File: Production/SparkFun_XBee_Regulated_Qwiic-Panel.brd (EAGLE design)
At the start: 127.8 x 177.8 mm, 870 parts, among them J13 QWIIC_RIGHT_ANGLE, J19 QWIIC_RIGHT_ANGLE, J25 QWIIC_RIGHT_ANGLE, J31 QWIIC_RIGHT_ANGLE, J37 QWIIC_RIGHT_ANGLE, J4 QWIIC_RIGHT_ANGLE, J43 QWIIC_RIGHT_ANGLE, J49 QWIIC_RIGHT_ANGLE, J7 QWIIC_RIGHT_ANGLE, U1 AP63203, U2 AP63203, U3 AP63203, U4 AP63203, U5 AP63203, U6 AP63203, U7 AP63203, U8 AP63203, U9 AP63203

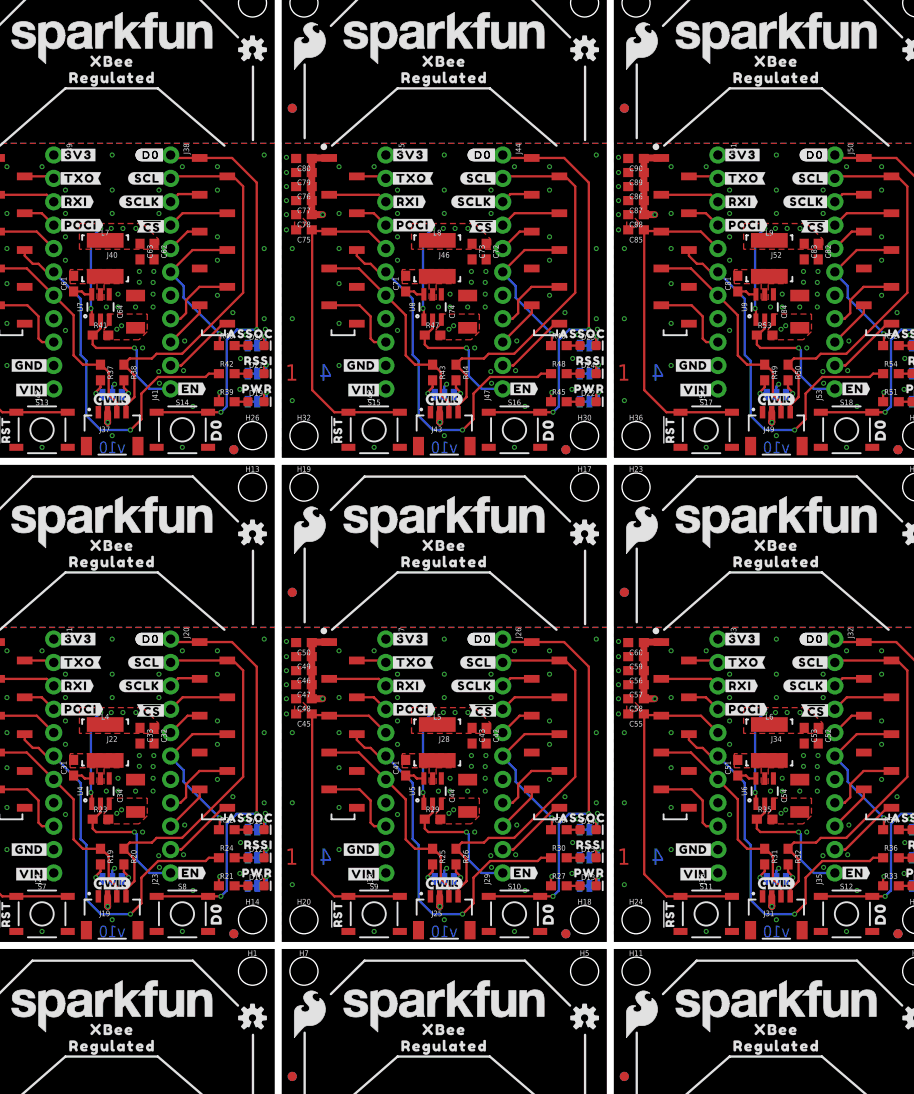
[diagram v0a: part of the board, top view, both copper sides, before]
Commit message: Updates silk on production files
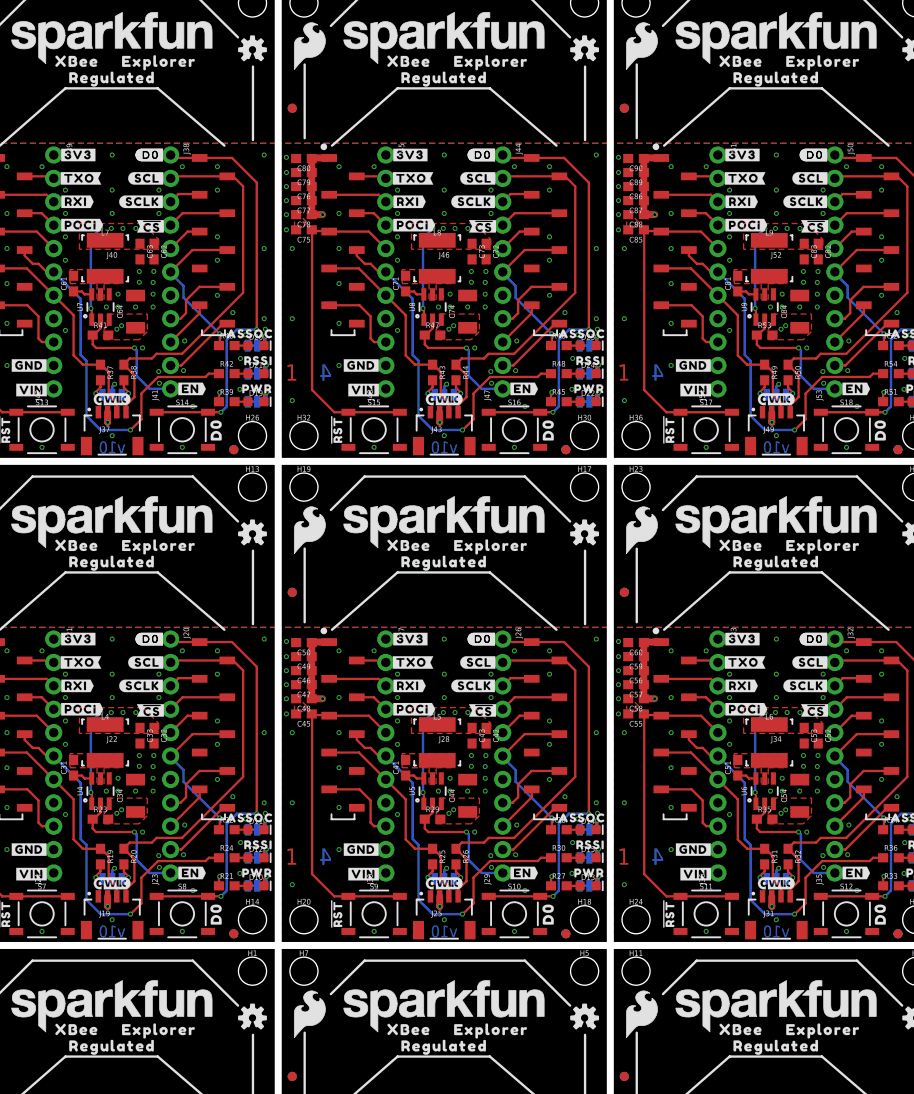
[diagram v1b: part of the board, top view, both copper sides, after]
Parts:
- added U$460: (no value), top:XBEE340
- added U$461: (no value), topmirror:REGULATED1343
- added U$462: (no value), botmirror:#D0#3
- added U$463: (no value), topmirror:#D1#AD1#SCL#8
- added U$464: (no value), topmirror:#RLED#22
- added U$465: (no value), topmirror:#D3#AD3##CS##23
- added U$466: (no value), topmirror:#EN#17
- added U$467, U$468: (no value), topmirror:EXPLORER1344
- U$103, U$260, U$311, U$33: device top:#3V3#1 -> topmirror:EXPLORER1344
- U$104, U$155: device top:#I2C#33 -> topmirror:EXPLORER1344
- U$105: device top:PWR26 -> top:#3V3#1
- U$106: device top:ASSOC27 -> top:#I2C#33
- U$107: device top:#3V3#1 -> top:PWR26
- U$108: device top:#VIN#4 -> top:ASSOC27
- U$109, U$313: device bot:D03 -> top:#3V3#1
- U$110: device top:#RST#30 -> top:#VIN#4
- U$111: device SparkFun-Aesthetics:SFE_LOGO_NAME_.2 -> bot:D03
- U$112: device SparkFun-Aesthetics:SFE_LOGO_FLAME_.2 -> top:#RST#30
- U$113: device top:RSSI31 -> SparkFun-Aesthetics:SFE_LOGO_NAME_.2
- U$114: device topmirror:#D0#AD0#18 -> SparkFun-Aesthetics:SFE_LOGO_FLAME_.2
- U$115: device topmirror:#D2#AD2#19 -> top:RSSI31
- U$116: device topmirror:#D6##RTS##25 -> topmirror:#D0#AD0#18
- U$117: device topmirror:#D5#ASSOC#25 -> topmirror:#D2#AD2#19
- U$118: device topmirror:#D9##SLP##28 -> topmirror:#D6##RTS##25
- U$119: device topmirror:#GND#0 -> topmirror:#D5#ASSOC#25
- U$120: device topmirror:#D8##DTR##27 -> topmirror:#D9##SLP##28
- U$121: device topmirror:#RSSI#D10#17 -> topmirror:#GND#0
- U$122: device topmirror:#SDA#D11#9 -> topmirror:#D8##DTR##27
- U$123: device topmirror:##RST##15 -> topmirror:#RSSI#D10#17
- U$124: device topmirror:#POCI#D12#24 -> topmirror:#SDA#D11#9
- U$125: device topmirror:#RXI#D14#15 -> topmirror:##RST##15
- U$126: device topmirror:#TXO#D13#13 -> topmirror:#POCI#D12#24
- U$127: device topmirror:#ALED#21 -> topmirror:#RXI#D14#15
- U$128: device topmirror:#PLED#20 -> topmirror:#TXO#D13#13
- U$129: device botmirror:#TXO#8 -> topmirror:#ALED#21
- U$130: device botmirror:#RXI#7 -> topmirror:#PLED#20
- U$131: device botmirror:#POCI#32 -> botmirror:#TXO#8
- U$132: device botmirror:##CS##26 -> botmirror:#RXI#7
- U$133: device botmirror:#SCLK#33 -> botmirror:#POCI#32
- U$134: device botmirror:#SCL#9 -> botmirror:##CS##26
- U$135: device botmirror:#D0#3 -> botmirror:#SCLK#33
- U$136: device top:#VIN#4 -> botmirror:#SCL#9
- U$137: device topmirror:#GND#0 -> botmirror:#D0#3
- U$138, U$162: device SparkFun-Aesthetics:SFE_LOGO_NAME_.2 -> top:#VIN#4
- U$139: device topmirror:#EN#17 -> topmirror:#GND#0
- U$140: device topmirror:#NC#1 -> SparkFun-Aesthetics:SFE_LOGO_NAME_.2
- U$141: device botmirror:#NC#3 -> topmirror:#EN#17
- U$142: device top:#D7##CTS##26 -> topmirror:#NC#1
- U$143: device top:#D4#PICO#25 -> botmirror:#NC#3
- U$144, U$352: device topmirror:REGULATED1343 -> top:#D7##CTS##26
- U$145, U$197, U$249: device top:XBEE340 -> top:#D4#PICO#25
- U$146, U$198, U$94: device top:XBEE340 -> topmirror:REGULATED1343
- U$148, U$199: device topmirror:REGULATED1343 -> top:XBEE340
- U$149, U$302: device botmirror:#D0#3 -> topmirror:REGULATED1343
- U$150: device topmirror:#D1#AD1#SCL#8 -> botmirror:#D0#3
- U$151: device topmirror:#RLED#22 -> topmirror:#D1#AD1#SCL#8
- U$152: device topmirror:#D3#AD3##CS##23 -> topmirror:#RLED#22
- U$153: device topmirror:#EN#17 -> topmirror:#D3#AD3##CS##23
- U$154, U$362: device top:#3V3#1 -> topmirror:#EN#17
- U$156, U$207: device top:PWR26 -> topmirror:EXPLORER1344
- U$157: device top:ASSOC27 -> top:#3V3#1
- U$158: device top:#3V3#1 -> top:#I2C#33
- U$159: device top:#VIN#4 -> top:PWR26
- U$160: device bot:D03 -> top:ASSOC27
- U$161, U$365: device top:#RST#30 -> top:#3V3#1
- U$163: device SparkFun-Aesthetics:SFE_LOGO_FLAME_.2 -> bot:D03
- U$164: device top:RSSI31 -> top:#RST#30
- U$165: device topmirror:#D0#AD0#18 -> SparkFun-Aesthetics:SFE_LOGO_NAME_.2
- U$166: device topmirror:#D2#AD2#19 -> SparkFun-Aesthetics:SFE_LOGO_FLAME_.2
- U$167: device topmirror:#D6##RTS##25 -> top:RSSI31
- U$168: device topmirror:#D5#ASSOC#25 -> topmirror:#D0#AD0#18
- U$169: device topmirror:#D9##SLP##28 -> topmirror:#D2#AD2#19
- U$170: device topmirror:#GND#0 -> topmirror:#D6##RTS##25
- U$171: device topmirror:#D8##DTR##27 -> topmirror:#D5#ASSOC#25
- U$172: device topmirror:#RSSI#D10#17 -> topmirror:#D9##SLP##28
- U$173: device topmirror:#SDA#D11#9 -> topmirror:#GND#0
- U$174: device topmirror:##RST##15 -> topmirror:#D8##DTR##27
- U$175: device topmirror:#POCI#D12#24 -> topmirror:#RSSI#D10#17
- U$176: device topmirror:#RXI#D14#15 -> topmirror:#SDA#D11#9
- U$177: device topmirror:#TXO#D13#13 -> topmirror:##RST##15
- U$178: device topmirror:#ALED#21 -> topmirror:#POCI#D12#24
- U$179: device topmirror:#PLED#20 -> topmirror:#RXI#D14#15
- U$180: device botmirror:#TXO#8 -> topmirror:#TXO#D13#13
- U$181: device botmirror:#RXI#7 -> topmirror:#ALED#21
- U$182: device botmirror:#POCI#32 -> topmirror:#PLED#20
- U$183: device botmirror:##CS##26 -> botmirror:#TXO#8
- U$184: device botmirror:#SCLK#33 -> botmirror:#RXI#7
- U$185: device botmirror:#SCL#9 -> botmirror:#POCI#32
- U$186: device botmirror:#D0#3 -> botmirror:##CS##26
- U$187: device top:#VIN#4 -> botmirror:#SCLK#33
- U$188: device topmirror:#GND#0 -> botmirror:#SCL#9
- U$189: device SparkFun-Aesthetics:SFE_LOGO_NAME_.2 -> botmirror:#D0#3
- U$190: device topmirror:#EN#17 -> top:#VIN#4
- U$191: device topmirror:#NC#1 -> topmirror:#GND#0
- U$192: device botmirror:#NC#3 -> SparkFun-Aesthetics:SFE_LOGO_NAME_.2
- U$193: device top:#D7##CTS##26 -> topmirror:#EN#17
- U$194: device top:#D4#PICO#25 -> topmirror:#NC#1
- U$195, U$403: device topmirror:REGULATED1343 -> botmirror:#NC#3
- U$196, U$248, U$300: device top:XBEE340 -> top:#D7##CTS##26
- U$200, U$251: device botmirror:#D0#3 -> top:XBEE340
- U$201, U$354: device topmirror:#D1#AD1#SCL#8 -> topmirror:REGULATED1343
- U$202: device topmirror:#RLED#22 -> botmirror:#D0#3
- U$203: device topmirror:#D3#AD3##CS##23 -> topmirror:#D1#AD1#SCL#8
- U$204: device topmirror:#EN#17 -> topmirror:#RLED#22
- U$205, U$413: device top:#3V3#1 -> topmirror:#D3#AD3##CS##23
- U$206: device top:#I2C#33 -> topmirror:#EN#17
- U$208, U$259: device top:ASSOC27 -> topmirror:EXPLORER1344
- U$210: device top:#VIN#4 -> top:#I2C#33
- U$211: device bot:D03 -> top:PWR26
- U$212: device top:#RST#30 -> top:ASSOC27
- U$213, U$417: device SparkFun-Aesthetics:SFE_LOGO_NAME_.2 -> top:#3V3#1
- U$214: device SparkFun-Aesthetics:SFE_LOGO_FLAME_.2 -> top:#VIN#4
- U$215: device top:RSSI31 -> bot:D03
- U$216: device topmirror:#D0#AD0#18 -> top:#RST#30
- U$217: device topmirror:#D2#AD2#19 -> SparkFun-Aesthetics:SFE_LOGO_NAME_.2
- U$218: device topmirror:#D6##RTS##25 -> SparkFun-Aesthetics:SFE_LOGO_FLAME_.2
- U$219: device topmirror:#D5#ASSOC#25 -> top:RSSI31
- U$220: device topmirror:#D9##SLP##28 -> topmirror:#D0#AD0#18
- U$221: device topmirror:#GND#0 -> topmirror:#D2#AD2#19
- U$222: device topmirror:#D8##DTR##27 -> topmirror:#D6##RTS##25
- U$223: device topmirror:#RSSI#D10#17 -> topmirror:#D5#ASSOC#25
- U$224: device topmirror:#SDA#D11#9 -> topmirror:#D9##SLP##28
- U$225: device topmirror:##RST##15 -> topmirror:#GND#0
- U$226: device topmirror:#POCI#D12#24 -> topmirror:#D8##DTR##27
- U$227: device topmirror:#RXI#D14#15 -> topmirror:#RSSI#D10#17
- U$228: device topmirror:#TXO#D13#13 -> topmirror:#SDA#D11#9
- U$229: device topmirror:#ALED#21 -> topmirror:##RST##15
- U$23: device top:XBEE340 -> topmirror:EXPLORER1344
- U$230: device topmirror:#PLED#20 -> topmirror:#POCI#D12#24
- U$231: device botmirror:#TXO#8 -> topmirror:#RXI#D14#15
- U$232: device botmirror:#RXI#7 -> topmirror:#TXO#D13#13
- U$233: device botmirror:#POCI#32 -> topmirror:#ALED#21
- U$234: device botmirror:##CS##26 -> topmirror:#PLED#20
- U$235: device botmirror:#SCLK#33 -> botmirror:#TXO#8
- U$236: device botmirror:#SCL#9 -> botmirror:#RXI#7
- U$237: device botmirror:#D0#3 -> botmirror:#POCI#32
- U$238: device top:#VIN#4 -> botmirror:##CS##26
- U$239: device topmirror:#GND#0 -> botmirror:#SCLK#33
- U$240: device SparkFun-Aesthetics:SFE_LOGO_NAME_.2 -> botmirror:#SCL#9
- U$241, U$306: device topmirror:#EN#17 -> botmirror:#D0#3
- U$242: device topmirror:#NC#1 -> top:#VIN#4
- U$243: device botmirror:#NC#3 -> topmirror:#GND#0
- U$244: device top:#D7##CTS##26 -> SparkFun-Aesthetics:SFE_LOGO_NAME_.2
- U$245: device top:#D4#PICO#25 -> topmirror:#EN#17
- U$246, U$454: device topmirror:REGULATED1343 -> topmirror:#NC#1
- U$247, U$299, U$351: device top:XBEE340 -> botmirror:#NC#3
- U$252, U$303: device topmirror:#D1#AD1#SCL#8 -> top:XBEE340
- U$253, U$406: device topmirror:#RLED#22 -> topmirror:REGULATED1343
- U$254: device topmirror:#D3#AD3##CS##23 -> botmirror:#D0#3
- U$255: device topmirror:#EN#17 -> topmirror:#D1#AD1#SCL#8
- U$256: device top:#3V3#1 -> topmirror:#RLED#22
- U$257: device top:#I2C#33 -> topmirror:#D3#AD3##CS##23
- U$258: device top:PWR26 -> topmirror:#EN#17
- U$261, U$47: device top:#VIN#4 -> top:#3V3#1
- U$262: device bot:D03 -> top:#I2C#33
- U$263: device top:#RST#30 -> top:PWR26
- U$264: device SparkFun-Aesthetics:SFE_LOGO_NAME_.2 -> top:ASSOC27
- U$265: device SparkFun-Aesthetics:SFE_LOGO_FLAME_.2 -> top:#3V3#1
- U$266: device top:RSSI31 -> top:#VIN#4
- U$267: device topmirror:#D0#AD0#18 -> bot:D03
- U$268: device topmirror:#D2#AD2#19 -> top:#RST#30
- U$269: device topmirror:#D6##RTS##25 -> SparkFun-Aesthetics:SFE_LOGO_NAME_.2
- U$270: device topmirror:#D5#ASSOC#25 -> SparkFun-Aesthetics:SFE_LOGO_FLAME_.2
- U$271: device topmirror:#D9##SLP##28 -> top:RSSI31
- U$272: device topmirror:#GND#0 -> topmirror:#D0#AD0#18
- U$273: device topmirror:#D8##DTR##27 -> topmirror:#D2#AD2#19
- U$274: device topmirror:#RSSI#D10#17 -> topmirror:#D6##RTS##25
- U$275: device topmirror:#SDA#D11#9 -> topmirror:#D5#ASSOC#25
- U$276: device topmirror:##RST##15 -> topmirror:#D9##SLP##28
- U$277: device topmirror:#POCI#D12#24 -> topmirror:#GND#0
- U$278: device topmirror:#RXI#D14#15 -> topmirror:#D8##DTR##27
- U$279: device topmirror:#TXO#D13#13 -> topmirror:#RSSI#D10#17
- U$280: device topmirror:#ALED#21 -> topmirror:#SDA#D11#9
- U$281: device topmirror:#PLED#20 -> topmirror:##RST##15
- U$282: device botmirror:#TXO#8 -> topmirror:#POCI#D12#24
- U$283: device botmirror:#RXI#7 -> topmirror:#RXI#D14#15
- U$284: device botmirror:#POCI#32 -> topmirror:#TXO#D13#13
- U$285: device botmirror:##CS##26 -> topmirror:#ALED#21
- U$286: device botmirror:#SCLK#33 -> topmirror:#PLED#20
- U$287: device botmirror:#SCL#9 -> botmirror:#TXO#8
- U$288: device botmirror:#D0#3 -> botmirror:#RXI#7
- U$289: device top:#VIN#4 -> botmirror:#POCI#32
- U$290: device topmirror:#GND#0 -> botmirror:##CS##26
- U$291: device SparkFun-Aesthetics:SFE_LOGO_NAME_.2 -> botmirror:#SCLK#33
- U$292: device topmirror:#EN#17 -> botmirror:#SCL#9
- U$293: device topmirror:#NC#1 -> botmirror:#D0#3
- U$294: device botmirror:#NC#3 -> top:#VIN#4
- U$295: device top:#D7##CTS##26 -> topmirror:#GND#0
- U$296: device top:#D4#PICO#25 -> SparkFun-Aesthetics:SFE_LOGO_NAME_.2
- U$297: device topmirror:REGULATED1343 -> topmirror:#EN#17
- U$298, U$350, U$402: device top:XBEE340 -> topmirror:#NC#1
- U$301, U$93: device topmirror:REGULATED1343 -> top:#D4#PICO#25
- U$304, U$355: device topmirror:#RLED#22 -> top:XBEE340
- U$305, U$458: device topmirror:#D3#AD3##CS##23 -> topmirror:REGULATED1343
- U$307: device top:#3V3#1 -> topmirror:#D1#AD1#SCL#8
- U$308: device top:#I2C#33 -> topmirror:#RLED#22
- U$309: device top:PWR26 -> topmirror:#D3#AD3##CS##23
- U$310: device top:ASSOC27 -> topmirror:#EN#17
- U$312, U$363: device top:#VIN#4 -> topmirror:EXPLORER1344
- U$314: device top:#RST#30 -> top:#I2C#33
- U$315: device SparkFun-Aesthetics:SFE_LOGO_NAME_.2 -> top:PWR26
- U$316: device SparkFun-Aesthetics:SFE_LOGO_FLAME_.2 -> top:ASSOC27
- U$317: device top:RSSI31 -> top:#3V3#1
- U$318: device topmirror:#D0#AD0#18 -> top:#VIN#4
- U$319: device topmirror:#D2#AD2#19 -> bot:D03
- U$320: device topmirror:#D6##RTS##25 -> top:#RST#30
- U$321: device topmirror:#D5#ASSOC#25 -> SparkFun-Aesthetics:SFE_LOGO_NAME_.2
- U$322: device topmirror:#D9##SLP##28 -> SparkFun-Aesthetics:SFE_LOGO_FLAME_.2
- U$323: device topmirror:#GND#0 -> top:RSSI31
- U$324: device topmirror:#D8##DTR##27 -> topmirror:#D0#AD0#18
- U$325: device topmirror:#RSSI#D10#17 -> topmirror:#D2#AD2#19
- U$326: device topmirror:#SDA#D11#9 -> topmirror:#D6##RTS##25
- U$327: device topmirror:##RST##15 -> topmirror:#D5#ASSOC#25
- U$328: device topmirror:#POCI#D12#24 -> topmirror:#D9##SLP##28
- U$329: device topmirror:#RXI#D14#15 -> topmirror:#GND#0
- U$330: device topmirror:#TXO#D13#13 -> topmirror:#D8##DTR##27
- U$331: device topmirror:#ALED#21 -> topmirror:#RSSI#D10#17
- U$332: device topmirror:#PLED#20 -> topmirror:#SDA#D11#9
- U$333: device botmirror:#TXO#8 -> topmirror:##RST##15
- U$334: device botmirror:#RXI#7 -> topmirror:#POCI#D12#24
- U$335: device botmirror:#POCI#32 -> topmirror:#RXI#D14#15
- U$336: device botmirror:##CS##26 -> topmirror:#TXO#D13#13
- U$337: device botmirror:#SCLK#33 -> topmirror:#ALED#21
- U$338: device botmirror:#SCL#9 -> topmirror:#PLED#20
- U$339: device botmirror:#D0#3 -> botmirror:#TXO#8
- U$340: device top:#VIN#4 -> botmirror:#RXI#7
- U$341: device topmirror:#GND#0 -> botmirror:#POCI#32
- U$342: device SparkFun-Aesthetics:SFE_LOGO_NAME_.2 -> botmirror:##CS##26
- U$343: device topmirror:#EN#17 -> botmirror:#SCLK#33
- U$344: device topmirror:#NC#1 -> botmirror:#SCL#9
- U$345: device botmirror:#NC#3 -> botmirror:#D0#3
- U$346: device top:#D7##CTS##26 -> top:#VIN#4
- U$347: device top:#D4#PICO#25 -> topmirror:#GND#0
- U$348: device topmirror:REGULATED1343 -> SparkFun-Aesthetics:SFE_LOGO_NAME_.2
- U$349, U$401, U$453: device top:XBEE340 -> topmirror:#EN#17
- U$353: device botmirror:#D0#3 -> top:#D4#PICO#25
- U$356, U$407: device topmirror:#D3#AD3##CS##23 -> top:XBEE340
- U$357: device topmirror:#EN#17 -> topmirror:REGULATED1343
- U$358: device top:#3V3#1 -> botmirror:#D0#3
- U$359: device top:#I2C#33 -> topmirror:#D1#AD1#SCL#8
- U$360: device top:PWR26 -> topmirror:#RLED#22
- U$361: device top:ASSOC27 -> topmirror:#D3#AD3##CS##23
- U$364, U$415: device bot:D03 -> topmirror:EXPLORER1344
- U$366: device SparkFun-Aesthetics:SFE_LOGO_NAME_.2 -> top:#I2C#33
- U$367: device SparkFun-Aesthetics:SFE_LOGO_FLAME_.2 -> top:PWR26
- U$368: device top:RSSI31 -> top:ASSOC27
- U$369: device topmirror:#D0#AD0#18 -> top:#3V3#1
- U$37: device top:#I2C#33 -> top:#3V3#1
- U$370: device topmirror:#D2#AD2#19 -> top:#VIN#4
- U$371: device topmirror:#D6##RTS##25 -> bot:D03
- U$372: device topmirror:#D5#ASSOC#25 -> top:#RST#30
- U$373: device topmirror:#D9##SLP##28 -> SparkFun-Aesthetics:SFE_LOGO_NAME_.2
- U$374: device topmirror:#GND#0 -> SparkFun-Aesthetics:SFE_LOGO_FLAME_.2
- U$375: device topmirror:#D8##DTR##27 -> top:RSSI31
- U$376: device topmirror:#RSSI#D10#17 -> topmirror:#D0#AD0#18
- U$377: device topmirror:#SDA#D11#9 -> topmirror:#D2#AD2#19
- U$378: device topmirror:##RST##15 -> topmirror:#D6##RTS##25
- U$379: device topmirror:#POCI#D12#24 -> topmirror:#D5#ASSOC#25
- U$38: device top:PWR26 -> top:#I2C#33
- U$380: device topmirror:#RXI#D14#15 -> topmirror:#D9##SLP##28
- U$381: device topmirror:#TXO#D13#13 -> topmirror:#GND#0
- U$382: device topmirror:#ALED#21 -> topmirror:#D8##DTR##27
- U$383: device topmirror:#PLED#20 -> topmirror:#RSSI#D10#17
- U$384: device botmirror:#TXO#8 -> topmirror:#SDA#D11#9
- U$385: device botmirror:#RXI#7 -> topmirror:##RST##15
- U$386: device botmirror:#POCI#32 -> topmirror:#POCI#D12#24
- U$387: device botmirror:##CS##26 -> topmirror:#RXI#D14#15
- U$388: device botmirror:#SCLK#33 -> topmirror:#TXO#D13#13
- U$389: device botmirror:#SCL#9 -> topmirror:#ALED#21
- U$39: device top:ASSOC27 -> top:PWR26
- U$390: device botmirror:#D0#3 -> topmirror:#PLED#20
- U$391: device top:#VIN#4 -> botmirror:#TXO#8
- U$392: device topmirror:#GND#0 -> botmirror:#RXI#7
- U$393: device SparkFun-Aesthetics:SFE_LOGO_NAME_.2 -> botmirror:#POCI#32
- U$394: device topmirror:#EN#17 -> botmirror:##CS##26
- U$395: device topmirror:#NC#1 -> botmirror:#SCLK#33
- U$396: device botmirror:#NC#3 -> botmirror:#SCL#9
- U$397: device top:#D7##CTS##26 -> botmirror:#D0#3
- U$398: device top:#D4#PICO#25 -> top:#VIN#4
- U$399: device topmirror:REGULATED1343 -> topmirror:#GND#0
- U$400, U$452: device top:XBEE340 -> SparkFun-Aesthetics:SFE_LOGO_NAME_.2
- U$404: device botmirror:#D0#3 -> top:#D7##CTS##26
- U$405: device topmirror:#D1#AD1#SCL#8 -> top:#D4#PICO#25
- U$408, U$459: device topmirror:#EN#17 -> top:XBEE340
- U$409: device top:#3V3#1 -> topmirror:REGULATED1343
- U$41: device top:#3V3#1 -> top:ASSOC27
- U$410: device top:#I2C#33 -> botmirror:#D0#3
- U$411: device top:PWR26 -> topmirror:#D1#AD1#SCL#8
- U$412: device top:ASSOC27 -> topmirror:#RLED#22
- U$414: device top:#VIN#4 -> topmirror:#EN#17
- U$416: device top:#RST#30 -> topmirror:EXPLORER1344
- U$418: device SparkFun-Aesthetics:SFE_LOGO_FLAME_.2 -> top:#I2C#33
- U$419: device top:RSSI31 -> top:PWR26
- U$420: device topmirror:#D0#AD0#18 -> top:ASSOC27
- U$421: device topmirror:#D2#AD2#19 -> top:#3V3#1
- U$422: device topmirror:#D6##RTS##25 -> top:#VIN#4
- U$423: device topmirror:#D5#ASSOC#25 -> bot:D03
- U$424: device topmirror:#D9##SLP##28 -> top:#RST#30
- U$425: device topmirror:#GND#0 -> SparkFun-Aesthetics:SFE_LOGO_NAME_.2
- U$426: device topmirror:#D8##DTR##27 -> SparkFun-Aesthetics:SFE_LOGO_FLAME_.2
- U$427: device topmirror:#RSSI#D10#17 -> top:RSSI31
- U$428: device topmirror:#SDA#D11#9 -> topmirror:#D0#AD0#18
- U$429: device topmirror:##RST##15 -> topmirror:#D2#AD2#19
- U$430: device topmirror:#POCI#D12#24 -> topmirror:#D6##RTS##25
- U$431: device topmirror:#RXI#D14#15 -> topmirror:#D5#ASSOC#25
- U$432: device topmirror:#TXO#D13#13 -> topmirror:#D9##SLP##28
- U$433: device topmirror:#ALED#21 -> topmirror:#GND#0
- U$434: device topmirror:#PLED#20 -> topmirror:#D8##DTR##27
- U$435: device botmirror:#TXO#8 -> topmirror:#RSSI#D10#17
- U$436: device botmirror:#RXI#7 -> topmirror:#SDA#D11#9
- U$437: device botmirror:#POCI#32 -> topmirror:##RST##15
- U$438: device botmirror:##CS##26 -> topmirror:#POCI#D12#24
- U$439: device botmirror:#SCLK#33 -> topmirror:#RXI#D14#15
- U$440: device botmirror:#SCL#9 -> topmirror:#TXO#D13#13
- U$441: device botmirror:#D0#3 -> topmirror:#ALED#21
- U$442: device top:#VIN#4 -> topmirror:#PLED#20
- U$443: device topmirror:#GND#0 -> botmirror:#TXO#8
- U$444: device SparkFun-Aesthetics:SFE_LOGO_NAME_.2 -> botmirror:#RXI#7
- U$445: device topmirror:#EN#17 -> botmirror:#POCI#32
- U$446: device topmirror:#NC#1 -> botmirror:##CS##26
- U$447: device botmirror:#NC#3 -> botmirror:#SCLK#33
- U$448: device top:#D7##CTS##26 -> botmirror:#SCL#9
- U$449: device top:#D4#PICO#25 -> botmirror:#D0#3
- U$450: device topmirror:REGULATED1343 -> top:#VIN#4
- U$451: device top:XBEE340 -> topmirror:#GND#0
- U$455: device botmirror:#D0#3 -> botmirror:#NC#3
- U$456: device topmirror:#D1#AD1#SCL#8 -> top:#D7##CTS##26
- U$457: device topmirror:#RLED#22 -> top:#D4#PICO#25
- U$48: device bot:D03 -> top:#VIN#4
- U$50: device top:#RST#30 -> bot:D03
- U$51: device SparkFun-Aesthetics:SFE_LOGO_NAME_.2 -> top:#RST#30
- U$53: device SparkFun-Aesthetics:SFE_LOGO_FLAME_.2 -> SparkFun-Aesthetics:SFE_LOGO_NAME_.2
- U$54: device top:RSSI31 -> SparkFun-Aesthetics:SFE_LOGO_FLAME_.2
- U$55: device topmirror:#D0#AD0#18 -> top:RSSI31
- U$56: device topmirror:#D2#AD2#19 -> topmirror:#D0#AD0#18
- U$57: device topmirror:#D6##RTS##25 -> topmirror:#D2#AD2#19
- U$58: device topmirror:#D5#ASSOC#25 -> topmirror:#D6##RTS##25
- U$67: device topmirror:#D9##SLP##28 -> topmirror:#D5#ASSOC#25
- U$68: device topmirror:#GND#0 -> topmirror:#D9##SLP##28
- U$69: device topmirror:#D8##DTR##27 -> topmirror:#GND#0
- U$70: device topmirror:#RSSI#D10#17 -> topmirror:#D8##DTR##27
- U$71: device topmirror:#SDA#D11#9 -> topmirror:#RSSI#D10#17
- U$72: device topmirror:##RST##15 -> topmirror:#SDA#D11#9
- U$73: device topmirror:#POCI#D12#24 -> topmirror:##RST##15
- U$74: device topmirror:#RXI#D14#15 -> topmirror:#POCI#D12#24
- U$75: device topmirror:#TXO#D13#13 -> topmirror:#RXI#D14#15
- U$76: device topmirror:#ALED#21 -> topmirror:#TXO#D13#13
- U$77: device topmirror:#PLED#20 -> topmirror:#ALED#21
- U$78: device botmirror:#TXO#8 -> topmirror:#PLED#20
- U$79: device botmirror:#RXI#7 -> botmirror:#TXO#8
- U$80: device botmirror:#POCI#32 -> botmirror:#RXI#7
- U$81: device botmirror:##CS##26 -> botmirror:#POCI#32
- U$82: device botmirror:#SCLK#33 -> botmirror:##CS##26
- U$83: device botmirror:#SCL#9 -> botmirror:#SCLK#33
- U$84: device botmirror:#D0#3 -> botmirror:#SCL#9
- U$85: device top:#VIN#4 -> botmirror:#D0#3
- U$86: device topmirror:#GND#0 -> top:#VIN#4
- U$87: device SparkFun-Aesthetics:SFE_LOGO_NAME_.2 -> topmirror:#GND#0
- U$88: device topmirror:#EN#17 -> SparkFun-Aesthetics:SFE_LOGO_NAME_.2
- U$89: device topmirror:#NC#1 -> topmirror:#EN#17
- U$90: device botmirror:#NC#3 -> topmirror:#NC#1
- U$91: device top:#D7##CTS##26 -> botmirror:#NC#3
- U$92: device top:#D4#PICO#25 -> top:#D7##CTS##26
- moved U$154 114.9 mm to (98.4, 7.62)
- moved U$307 103.6 mm to (101.9, 83.1), flipped to the bottom
- moved U$308 97.0 mm to (101.7, 61.8)
- moved U$311 96.1 mm to (95.0, 95.8), flipped to the top
- moved U$310 88.0 mm to (98.4, 60.2)
- moved U$155 78.6 mm to (95.0, 43.2), flipped to the top
- moved U$312 77.7 mm to (84.8, 95.8)
- moved U$309 76.6 mm to (101.7, 77.9), flipped to the bottom
- moved U$364 66.0 mm to (12.7, 148.3), flipped to the bottom, turned to 0 degrees
- moved U$208 63.5 mm to (12.7, 95.8), flipped to the bottom
- moved U$207 58.7 mm to (22.9, 95.8)
- moved U$415 58.2 mm to (58.9, 148.3), turned to 0 degrees
- moved U$104 56.0 mm to (48.8, 43.2)
- moved U$259 54.7 mm to (58.9, 95.8)
- moved U$156 54.1 mm to (84.8, 43.2), flipped to the bottom
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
